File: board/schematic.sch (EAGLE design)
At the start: 41 parts, among them IC1 STM32F207ZGT, IC3 LM3940, J1 DCJ0202, J3 DM3AT-SF-PEJM5

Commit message: Board w/ more measures; final version is still on my computer
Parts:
- removed JP3: (no value), con-lstb:MA06-1
- added J4: (no value), pinhead:PINHD-2X8
- JP1: device pinhead:PINHD-2X8 -> pinhead:PINHD-1X5
- JP2: device con-lstb:MA05-1 -> con-lstb:MA06-1
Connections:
- net +3V3: now also JP1.1; no longer JP3.1
- net A: now also J4.9; no longer JP1.9
- net B: now also J4.10; no longer JP1.10
- net B0: now also J4.3; no longer JP1.3
- net B1: now also J4.7; no longer JP1.7
- net C: now also J4.11; no longer JP1.11
- net D: now also J4.12; no longer JP1.12
- net DCLK: now also J4.13; no longer JP1.13
- net DEBUG_TX: now also JP1.5; no longer JP2.5
- net ESP_PROG_RX: now also JP1.3; no longer JP2.3
- net ESP_PROG_TX: now also JP1.2; no longer JP2.2
- net G0: now also J4.2; no longer JP1.2
- net G1: now also J4.6; no longer JP1.6
- net GND: now also J4.16, J4.4, J4.8, JP2.3; no longer JP1.16, JP1.8, JP2.4, JP3.3
- net LAT: now also J4.14; no longer JP1.14
- net OE: now also J4.15; no longer JP1.15
- net R0: now also J4.1; no longer JP1.1
- net R1: now also J4.5; no longer JP1.5
- net RESET: now also JP2.5; no longer JP3.5
- net SWCLK: now also JP2.2; no longer JP3.2
- net SWDIO: now also JP2.4; no longer JP3.4
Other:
- note added: "LOW ESR"

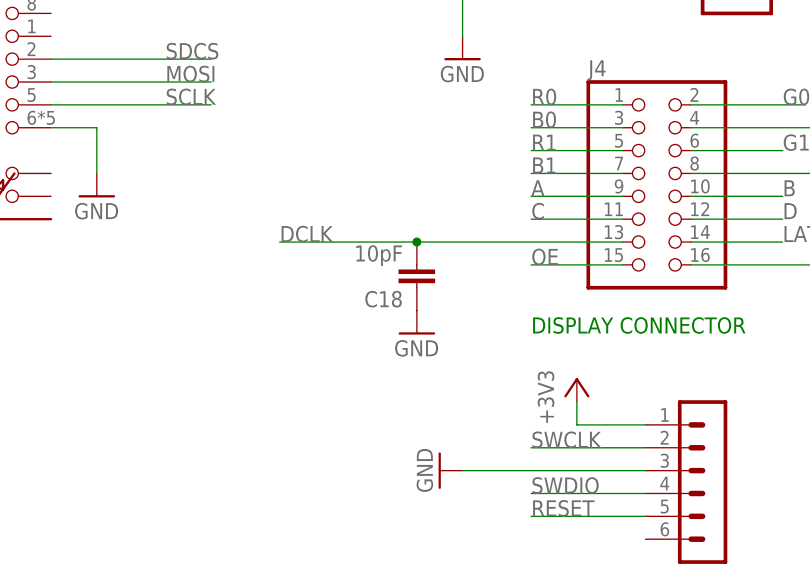
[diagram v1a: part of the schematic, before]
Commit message: Update board to REV B
Fixes noise issues -- workaround: use a 470k resistor on C18 instead of
the cap.
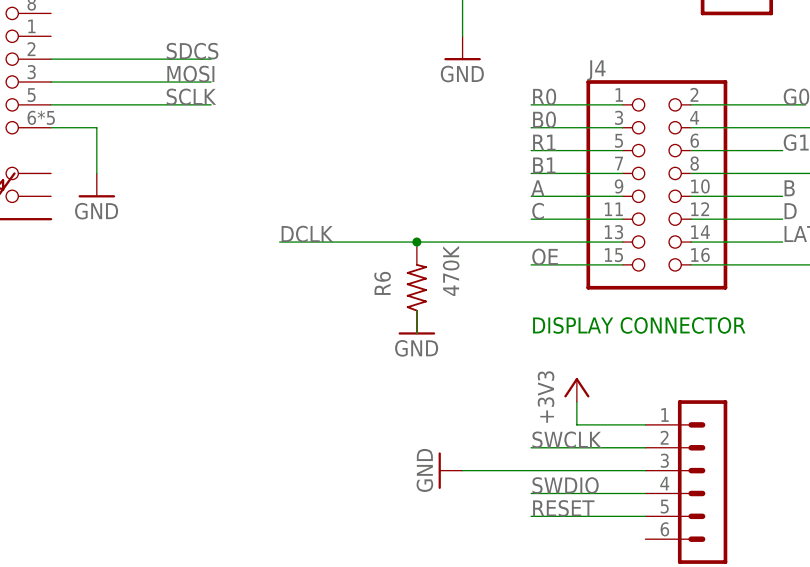
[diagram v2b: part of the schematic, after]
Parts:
- removed C18: 10pF, rcl:C-EU050-024X044
- added R6: 470K, rcl:R-US_0204/7
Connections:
- net DCLK: now also R6.2; no longer C18.2
- net GND: now also R6.1; no longer C18.1
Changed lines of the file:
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@@
 <part name="GND4" library="supply1" library_urn="urn:adsk.eagle:library:371" deviceset="GND" device=""/>
 <part name="J3" library="connector" deviceset="DM3AT-SF-PEJM5" device=""/>
-<part name="C18" library="rcl" library_urn="urn:adsk.eagle:library:334" deviceset="C-EU" device="050-024X044" package3d_urn="urn:adsk.eagle:package:23643/1" value="10pF"/>
+<part name="R6" library="rcl" library_urn="urn:adsk.eagle:library:334" deviceset="R-US_" device="0204/7" package3d_urn="urn:adsk.eagle:package:23498/1" value="470K"/>
 <part name="GND21" library="supply1" library_urn="urn:adsk.eagle:library:371" deviceset="GND" device=""/>
 <part name="J2" library="SparkFun-Connectors" deviceset="CONN_02" device="5MM"/>
@@
 <attribute name="VALUE" x="205.74" y="68.58" size="1.27" layer="96"/>
 </instance>
-<instance part="C18" gate="G$1" x="274.32" y="63.5" smashed="yes" rot="R180">
-<attribute name="NAME" x="272.796" y="63.119" size="1.778" layer="95" rot="R180"/>
-<attribute name="VALUE" x="272.796" y="68.199" size="1.778" layer="96" rot="R180"/>
+<instance part="R6" gate="G$1" x="274.32" y="63.5" smashed="yes" rot="R90">
+<attribute name="NAME" x="271.399" y="62.484" size="1.778" layer="95" rot="R90"/>
+<attribute name="VALUE" x="279.019" y="62.484" size="1.778" layer="96" rot="R90"/>
 </instance>
 <instance part="GND21" gate="1" x="274.32" y="58.42" smashed="yes">
@@
 <segment>
 <pinref part="J4" gate="A" pin="13"/>
-<pinref part="C18" gate="G$1" pin="2"/>
+<pinref part="R6" gate="G$1" pin="2"/>
 <wire x1="297.18" y1="68.58" x2="274.32" y2="68.58" width="0.1524" layer="91"/>
 <wire x1="274.32" y1="68.58" x2="259.08" y2="68.58" width="0.1524" layer="91"/>
@@
 </segment>
 <segment>
-<pinref part="C18" gate="G$1" pin="1"/>
+<pinref part="R6" gate="G$1" pin="1"/>
 <pinref part="GND21" gate="1" pin="GND"/>
-</segment>
-<segment>
+<wire x1="274.32" y1="60.96" x2="274.32" y2="58.42" width="0.1524" layer="91"/>
+</segment>
+<segment>

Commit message: bord redisgn
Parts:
- removed C10, C11, C12, C13, C14, C15, C16, C17, C8, C9: 100nF, rcl:C-EU025-025X050
- removed IC1: STM32F207ZGT, micro-stm_v3:STM32F207ZGT
- added IC4: STM32F205RGT, micro-stm_v3:STM32F205RGT
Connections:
- new net N$4: C1.2, C2.2, C3.2, IC4MCU.VBAT, IC4MCU.VDDA
- net +3V3: now also IC4PWR.VDD@1, IC4PWR.VDD@2, IC4PWR.VDD@3, IC4PWR.VDD@4; no longer C1.2, C10.1, C11.1, C12.1, C13.1, C14.1, C15.1, C16.1, C17.1, C2.2, C3.2, C8.1, C9.1, IC1MCU.VBAT, IC1MCU.VDDA, IC1MCU.VREF+, IC1PWR.VDD@1, IC1PWR.VDD@10, IC1PWR.VDD@11, IC1PWR.VDD@12, IC1PWR.VDD@2, IC1PWR.VDD@3, IC1PWR.VDD@4, IC1PWR.VDD@5, IC1PWR.VDD@6, IC1PWR.VDD@7, IC1PWR.VDD@8, IC1PWR.VDD@9
- net A: now also IC4MCU.PB0; no longer IC1MCU.PB0
- net B: now also IC4MCU.PB1; no longer IC1MCU.PB1
- net B0: now also IC4MCU.PC2; no longer IC1MCU.PD2
- net B1: now also IC4MCU.PC5; no longer IC1MCU.PD5
- net C: now also IC4MCU.PB2; no longer IC1MCU.PB2
- net D: now also IC4MCU.PB3; no longer IC1MCU.PB3
- net DCLK: now also IC4MCU.PC6; no longer IC1MCU.PD6
- net G0: now also IC4MCU.PC1; no longer IC1MCU.PD1
- net G1: now also IC4MCU.PC4; no longer IC1MCU.PD4
- net GND: now also IC4MCU.BOOT0, IC4MCU.VSSA, IC4PWR.VSS@1, IC4PWR.VSS@2; no longer C10.2, C11.2, C12.2, C13.2, C14.2, C15.2, C16.2, C17.2, C8.2, C9.2, IC1MCU.BOOT0, IC1MCU.VSSA, IC1PWR.VSS@1, IC1PWR.VSS@2, IC1PWR.VSS@3, IC1PWR.VSS@4, IC1PWR.VSS@5, IC1PWR.VSS@6, IC1PWR.VSS@7, IC1PWR.VSS@8, IC1PWR.VSS@9
- net LAT: now also IC4MCU.PB5; no longer IC1MCU.PB5
- net N$2: now also IC4MCU.VCAP1; no longer IC1MCU.VCAP2
- net N$3: now also IC4MCU.VCAP2; no longer IC1MCU.VCAP1
- net OE: now also IC4MCU.PB6; no longer IC1MCU.PB6
- net R0: now also IC4MCU.PC0; no longer IC1MCU.PD0
- net R1: now also IC4MCU.PC3; no longer IC1MCU.PD3
- net RESET: now also IC4MCU.NRST; no longer IC1MCU.NRST
- net RX: now also IC4MCU.PA3; no longer IC1MCU.PG9
- net SWCLK: now also IC4MCU.PA14; no longer IC1MCU.PA14
- net SWDIO: now also IC4MCU.PA13; no longer IC1MCU.PA13
- net TX: now also IC4MCU.PA2; no longer IC1MCU.PG14
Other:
- moved on the sheet: C1, C2, C3, C4, C5, C6, C7

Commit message: c
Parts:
- removed J4: (no value), pinhead:PINHD-2X8
- added IC1, IC5: 74HCT244DW, 74xx-eu:74HCT244DW
- added J5: (no value), pinhead:PINHD-2X8
- R6: value 470K -> 470k
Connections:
- new net A_H: IC1B.Y1, J5.9
- new net B0_H: IC1A.Y2, J5.3
- new net B1_H: IC1A.Y4, J5.7
- new net B_H: IC5A.Y3, J5.10
- new net C_H: IC1B.Y2, J5.11
- new net DCLK_H: IC1B.Y3, J5.13, R6.2
- new net D_H: IC5A.Y4, J5.12
- new net G0_H: IC5A.Y1, J5.2
- new net G1_H: IC5A.Y2, J5.6
- new net LAT_H: IC5B.Y1, J5.14
- new net OE_H: IC1B.Y4, J5.15
- new net R0_H: IC1A.Y1, J5.1
- new net R1_H: IC1A.Y3, J5.5
- net +5V: now also IC1P.VCC, IC5P.VCC
- net A: now also IC1B.A1; no longer J4.9
- net B: now also IC5A.A3; no longer J4.10
- net B0: now also IC1A.A2; no longer J4.3
- net B1: now also IC1A.A4; no longer J4.7
- net C: now also IC1B.A2; no longer J4.11
- net D: now also IC5A.A4; no longer J4.12
- net DCLK: now also IC1B.A3; no longer J4.13, R6.2
- net G0: now also IC5A.A1; no longer J4.2
- net G1: now also IC5A.A2; no longer J4.6
- net GND: now also IC1A.G, IC1B.G, IC1P.GND, IC5A.G, IC5B.G, IC5P.GND, J5.16, J5.4, J5.8; no longer J4.16, J4.4, J4.8
- net LAT: now also IC5B.A1; no longer J4.14
- net OE: now also IC1B.A4; no longer J4.15
- net R0: now also IC1A.A1; no longer J4.1
- net R1: now also IC1A.A3; no longer J4.5
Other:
- note removed: "DISPLAY CONNECTOR"
- moved on the sheet: JP2, R6

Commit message: board rev b minus button board connectors
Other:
- note added: "3V3 REGULATOR"
- note added: "B"
- note added: "BARREL JACK"
- note added: "BUTTONS"
- note added: "DISPLAY DATA CONNECTOR"
- note added: "External connectors and sockets"
- note added: "LL CONVERTER POWER"
- note added: "MICROSD CARD"
- note added: "MSign"
- note added: "Power pins and on-board buttons"
- note added: "STM POWER PINS"
- note added: "STM PROGRAMMING HEADER"
- note added: "STM32 and ESP8266 wiring."
- note removed: "MCU POWER"
- note removed: "POWER"
- note removed: "SD CARD"
- note removed: "SWD CONNECTOR"
